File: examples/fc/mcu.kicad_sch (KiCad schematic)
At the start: 18 parts, among them J2 USB-C, J3 SWD, U3 STM32F405RGT6, Y1 8MHz

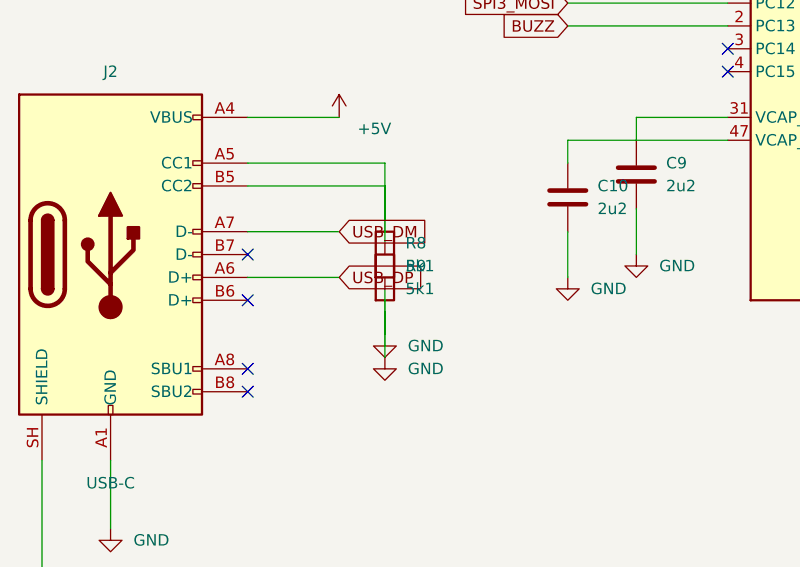
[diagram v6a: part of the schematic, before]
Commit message: Rebuild fc's pages after the R8/R9 fix
The two 5k1 pulldowns moved into separate columns, so the MCU page and the
UUIDs regenerated with it. Design unchanged: 0 errors, 0 warnings, 76 nets,
46 named.
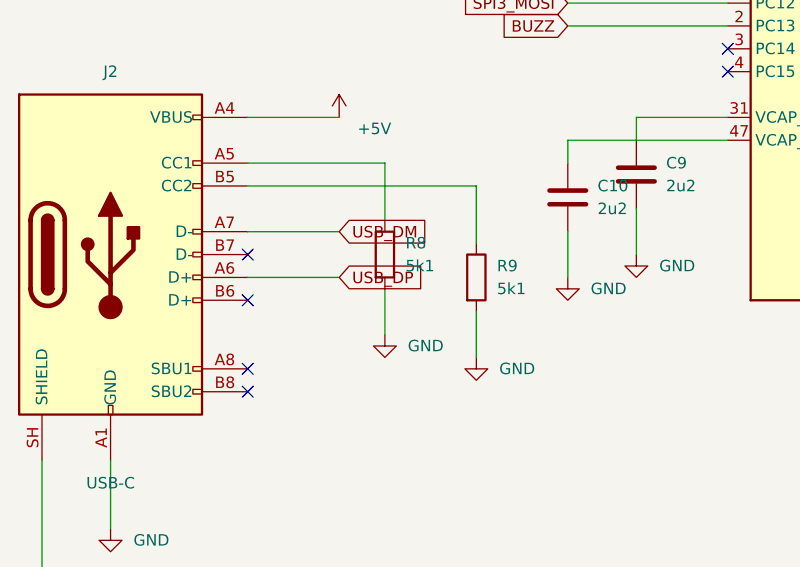
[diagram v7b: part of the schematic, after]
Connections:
- net at J2.A5 (CC1), R8.1: no longer J2.B5 (CC2), R9.1
- new net: J2.B5 (CC2), R9.1
